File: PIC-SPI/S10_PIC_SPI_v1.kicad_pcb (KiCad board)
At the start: 2 copper layers, 254 x 134.1 mm, 164 parts, among them P1 M25P80 ISP, P10 CONN_4, P19 XILINX CABLE2, P2 CONN_4, P3 CONN_2, P4 S100_MALE, P5 PIC_ISP, P6 CONN_1, P7 CONN_1, P8 CONN_2, P9 CONN_2, Q1 ^^NPN-SOT23, Q2 ^^NPN-SOT23, Q3 ^^NPN-SOT23, Q4 ^^NPN-SOT23, Q5 ^^NPN-SOT23, Q6 ^^NPN-SOT23, Q7 ^^NPN-SOT23, Q8 ^^NPN-SOT23, Q9 ^^NPN-SOT23, SW1 RESET, SW2 RESET, SW4 FLASH_SELECT, SW50 FLASH/RUN, U1 LDO_REG_7805, U11 ^^74LS541, U12 ^^74LV244, U14 M25P80, U15 M25P80, U16 M25P80, U17 M25P80, U18 CH341A, U19 ^^74LS541, U2 LM1086CS, U20 XC95288XL-TQ144, U3din1 ^^74LS541, U3dout1 ^^74LS541, U4 ^^74LS541, U5 ^^74LS541, U6 ^^74LS541, U7a1 74HC245, U7b1 74HC245, U8 PIC18F1330, X1 12MHz

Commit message: PIC-SPI: annotate, add 7-segment displays (2x 74HC4511), read netlist into the PCB
Source: S100 PIC_SPI_v1/backups/06-01-2016 1810
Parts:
- removed Cx15: 0.1 uF, C2
- removed D13: POWER FT232R, ^^LED-0805
- removed D14: TMA0, ^^LED-0805
- removed D15: TMA1, ^^LED-0805
- removed D16: TMA2, ^^LED-0805
- removed D17: TMA3, ^^LED-0805
- removed D6: DONE, ^^LED-0805
- removed Dx2, Dx3: LED, ^^LED-0805
- removed JP4, JP5: JUMPER, PIN_ARRAY_2X1
- removed Jx1: USB_2, USB_A
- removed Kx1: CONN_3, SIL-3
- removed P3: CONN_2, SIL-2
- removed Px12: CLK_UART, DIP-14__300_ELL
- removed Q3, Q4, Q5, Q6, Q7, Q8, Q9: ^^NPN-SOT23, ^^-SOT23
- removed R45, Rx7, Rx8: 330, ^^SMD_Resistor-0805
- removed R46, R47: 470, ^^SMD_Resistor-0805
- removed Rx2: 4700, ^^SMD_Resistor-0805
- removed SW4: FLASH_SELECT, SW_PUSH_SMALL
- removed SWx2: DIPS_08, 16dip300
- removed U7a1, U7b1: 74HC245, ^^-SO20W
- removed Ux17: 74LS682N, 20DIP-ELL300
- removed Ux18: 16550, DIP-40__600_ELL
- removed Ux21: FT232R, -SSOP28
- added BAT1: CR2032, CR2032H, F.Cu at (165.0, 122.4)
- added C13: 0.01 uF, ^^SMD_Resistor-0805, B.Cu at (266.5, 101.6)
- added C16: 0.1 uF, C2, F.Cu at (158.6, 186.6)
- added C22: 0.1 uF, C2, F.Cu at (181.6, 150.3)
- added C23: 0.1 uF, C2, F.Cu at (125.2, 99.6)
- added C24: 0.1 uF, C2, F.Cu at (124.7, 186.5)
- added C29: 0.1 uF, C2, F.Cu at (124.8, 172.4)
- added C30: 0.1 uF, C2, F.Cu at (181.6, 165.3)
- added C31: 0.1 uF, ^^SMD_Resistor-0805, F.Cu at (200.3, 183.6)
- added C32: 0.1 uF, C2, F.Cu at (152.4, 143.9)
- added C41: 0.1 uF, ^^SMD_Resistor-0805, B.Cu at (227.6, 183.9)
- added C42: 0.1 uF, ^^SMD_Resistor-0805, B.Cu at (290.3, 199.5)
- added C43: 0.1 uF, ^^SMD_Resistor-0805, B.Cu at (290.4, 182.4)
- added IC1: MCP23S08SO, DIP-18__300_ELL, F.Cu at (195.9, 165.4)
- added IC2: MCP23S08SO, DIP-18__300_ELL, F.Cu at (195.9, 150.3)
- added JP1: JUMPER, SIL-2, F.Cu at (178.7, 201.4)
- added MCP1: CONN_3X2, PIN_ARRAY_3X2, F.Cu at (175.6, 156.7)
- added MCP2: CONN_3X2, PIN_ARRAY_3X2, F.Cu at (175.5, 164.4)
- added P11: CONN_3X2, PIN_ARRAY_3X2, F.Cu at (163.4, 174.8)
- added P12: CONN_8X2, pin_array_8x2, F.Cu at (139.9, 201.4)
- added P13: MCP_1, SIL-10, F.Cu at (190.7, 91.4)
- added P14: MCP_2, SIL-10, F.Cu at (190.7, 97.1)
- added RR1: 1000, r_pack9, F.Cu at (141.1, 107.6)
- added S1: 7SEGM, ^^VQB71_7segment, F.Cu at (310.0, 175.3)
- added S2: 7SEGM, ^^VQB71_7segment, F.Cu at (319.4, 175.2)
- added SW3: DIPS_08, SWDIP8, F.Cu at (110.1, 144.1)
- added SW5: DIPS_08, SWDIP8, F.Cu at (137.1, 144.2)
- added SW6: DIPS_08, SWDIP8, F.Cu at (109.7, 103.8)
- added U10: 74HC245, ^^-SO20W, F.Cu at (249.4, 183.8)
- added U13: 74LS244, DIP-20__300_ELL, F.Cu at (140.7, 99.6)
- added U21: 74LS240, DIP-20__300_ELL, F.Cu at (140.3, 186.7)
- added U22: DS1305, DIP-16__300_ELL, F.Cu at (165.4, 143.9)
- added U23: M25P80, -SO8, F.Cu at (296.2, 157.5)
- added U24: M25P80, -SO8, F.Cu at (304.6, 157.5)
- added U25: M25P80, -SO8, F.Cu at (312.8, 157.5)
- added U26: M25P80, -SO8, F.Cu at (320.8, 157.5)
- added U27: 74HC4511, ^^-SO16W, B.Cu at (290.2, 175.1)
- added U28: 74HC4511, ^^-SO16W, B.Cu at (290.1, 192.3)
- added U3: 74LS682N, DIP-20__300_ELL, F.Cu at (140.3, 158.2)
- added U30: 74HC04, DIP-14__300_ELL, F.Cu at (170.4, 186.6)
- added U31: ^^74LS541, ^^-SO20W, F.Cu at (208.5, 183.9)
- added U7: 74LS682N, DIP-20__300_ELL, F.Cu at (140.3, 172.5)
- added U9: 74HC245, ^^-SO20W, F.Cu at (228.2, 183.9)
- added X2: CRYSTAL, Crystal_HC-49U_Horiz, F.Cu at (163.7, 152.7)
- C10, C15, C18: moved to B.Cu
- C17, C20, C21, C25, C27, C28, C4, C8: footprint C2 -> ^^SMD_Resistor-0805
- D10: value FLASH_1 -> D1
- D11: value FLASH_2 -> D4
- D12: value FLASH_3 -> D5
- D2: value P55 -> D2
- D3: value P54 -> D3
- D9: value FLASH_0 -> D0
- R11: value 10k -> 1K; footprint ^^SMD_Resistor-0805 -> ^^R3; moved to F.Cu
- R31, R33, R35, R37, R39: value 330 -> 1K
- R32, R34, R36, R38: value 470 -> 1K
- R40, R41, R42, R43, R44: value 330 -> 1K; moved to B.Cu
- R6: value 330 -> 1K; footprint ^^SMD_Resistor-0805 -> ^^R3; moved to F.Cu
- R7: value 470 -> 50
- U11: value ^^74LS541 -> 8259A; footprint ^^-SO20W -> DIP-28__600_ELL
- U14: footprint 8DIP-ELL300 -> -SO8
- U15, U16, U17: moved to F.Cu
- U18: footprint -SO28W -> ^^-SO28W
- U3din1, U3dout1: value ^^74LS541 -> ^^74HC541
- moved R31 180.9 mm to (302.2, 177.3)
- moved R33 168.7 mm to (302.2, 172.8), turned to 180 degrees
- moved R32 167.7 mm to (302.2, 175.1), turned to 180 degrees
- moved R39 166.4 mm to (301.9, 191.9), turned to 180 degrees
- moved R38 164.3 mm to (301.9, 194.1), turned to 180 degrees
- moved R37 164.0 mm to (302.2, 179.5), turned to 180 degrees
- moved R35 162.6 mm to (302.2, 168.4), turned to 180 degrees
- moved R36 162.4 mm to (302.2, 181.7), turned to 180 degrees
- moved R34 161.6 mm to (302.2, 170.6), turned to 180 degrees
- moved P19 147.2 mm to (233.8, 93.0), turned to 180 degrees
- moved R40 145.2 mm to (302.0, 189.6), turned to 180 degrees
- moved R27 143.5 mm to (236.4, 98.4), turned to 90 degrees
- moved R41 142.8 mm to (302.0, 187.4), turned to 180 degrees
- moved R25 141.2 mm to (233.8, 98.4), turned to 90 degrees
- moved R42 140.5 mm to (302.0, 185.2), turned to 180 degrees
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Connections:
- net /DI0b renamed /DI0
- net /DI1b renamed /DI1
- net /DI2b renamed /DI2
- net /DI3b renamed /DI3
- net /DI4b renamed /DI4
- net /DI5b renamed /DI5
- net /DI6b renamed /DI6
- net /DI7b renamed /DI7
- net /DO0b renamed /DO0
- net /DO1b renamed /DO1
- net /DO2b renamed /DO2
- net /DO3b renamed /DO3
- net /DO4b renamed /DO4
- net /DO5b renamed /DO5
- net /DO6b renamed /DO6
- net /DO7b renamed /DO7
- net /FLASH_0 renamed /LED_D0
- net /FLASH_1 renamed /LED_D1
- C14 pad 1: /V3.3b -> GND
- C14 pad 2: GND -> N-00000116
- C19 pad 1: /V3.3 -> /V3.3_CLPD_IO
- C26 pad 1: /V3.3 -> /V3.3_CLPD_INT
- C33 pad 1: /V3.3 -> /V3.3_CLPD_INT
- C34 pad 1: /V3.3 -> /V3.3_CLPD_IO
- C35 pad 1: /V3.3 -> /V3.3_CLPD_IO
- C36 pad 1: /V3.3 -> /V3.3_CLPD_IO
- C37 pad 1: /V3.3 -> /V3.3_CLPD_IO
- C38 pad 1: /V3.3 -> /V3.3_CLPD_IO
- C39 pad 1: /V3.3 -> /V3.3_CLPD_IO
- C40 pad 1: /V3.3 -> /V3.3_CLPD_IO
- D11 pad 1: /FLASH_2 -> /LED_D4
- D12 pad 1: /FLASH_3 -> /LED_D5
- D2 pad 1: N-00000404 -> /LED_D2
- D2 pad 2: GND -> N-00000211
- D3 pad 1: N-00000407 -> /LED_D3
- D3 pad 2: GND -> N-00000212
- D7 pad 1: N-00000403 -> /BOARD_SEL_LED
- D7 pad 2: GND -> N-00000256
- JPx1 pad 2: /BOARD_INTERRUPT_VECTc -> /BOARD_INTERRUPT_VECTb
- JPx2 pad 2: /BOARD_INTERRUPT_VECTc -> /BOARD_INTERRUPT_VECTb
- JPx3 pad 2: /BOARD_INTERRUPT_VECTc -> /BOARD_INTERRUPT_VECTb
- JPx4 pad 2: /BOARD_INTERRUPT_VECTc -> /BOARD_INTERRUPT_VECTb
- JPx5 pad 2: /BOARD_INTERRUPT_VECTc -> /BOARD_INTERRUPT_VECTb
- JPx6 pad 2: /BOARD_INTERRUPT_VECTc -> /BOARD_INTERRUPT_VECTb
- JPx7 pad 2: /BOARD_INTERRUPT_VECTc -> /BOARD_INTERRUPT_VECTb
- JPx8 pad 2: /BOARD_INTERRUPT_VECTc -> /BOARD_INTERRUPT_VECTb
- P4 pad 15: /A18b -> /A18
- P4 pad 16: /A16b -> /A16
- P4 pad 17: /A17b -> /A17
- P4 pad 29: /A5b -> /A5
- P4 pad 30: /A4b -> /A4
- P4 pad 31: /A3b -> /A3
- P4 pad 32: /A15b -> /A15
- P4 pad 33: /A12b -> /A12
- P4 pad 34: /A9b -> /A9
- P4 pad 37: /A10b -> /A10
- P4 pad 58: (no net) -> /sXTRQ*
- P4 pad 59: /A19b -> /A19
- P4 pad 61: /A20b -> /A20
- P4 pad 62: /A21b -> /A21
- P4 pad 63: /A22b -> /A22
- P4 pad 64: /A23b -> /A23
- P4 pad 72: /RDY -> (no net)
- P4 pad 73: (no net) -> /INT*
- P4 pad 79: /A0b -> /A0
- P4 pad 80: /A1b -> /A1
- P4 pad 81: /A2b -> /A2
- P4 pad 82: /A6b -> /A6
- P4 pad 83: /A7b -> /A7
- P4 pad 84: /A8b -> /A8
- P4 pad 85: /A13b -> /A13
- P4 pad 86: /A14b -> /A14
- P4 pad 87: /A11b -> /A11
- P4 pad 96: (no net) -> /sINTA
- P8 pad 1: /V3.3 -> /V3.3_CLPD_INT
- P9 pad 1: /V3.3 -> /V3.3_CLPD_IO
- R11 pad 2: N-00000274 -> N-00000236
- R13 pad 1: N-00000404 -> GND
- R13 pad 2: /LED_D2 -> N-00000211
- R15 pad 1: N-00000228 -> GND
- R16 pad 1: N-00000407 -> GND
- R16 pad 2: /LED_D3 -> N-00000212
- R20 pad 1: N-00000403 -> GND
- R20 pad 2: /BOARD_SEL_LED -> N-00000256
- R31 pad 2: GND -> N-00000221
- R32 pad 1: /TMA0* -> N-00000271
- R33 pad 2: VCC -> N-00000244
- R34 pad 1: /TMA1* -> N-00000263
- R35 pad 2: VCC -> N-00000245
- R36 pad 1: /TMA2* -> N-00000265
- R37 pad 2: VCC -> N-00000247
- R38 pad 1: /TMA3* -> N-00000258
- R39 pad 2: VCC -> N-00000250
- R40 pad 1: /TMA0* -> N-00000269
- R40 pad 2: VCC -> N-00000251
- R41 pad 1: /TMA1* -> N-00000268
- R41 pad 2: VCC -> N-00000252
- R42 pad 1: /TMA2* -> N-00000267
- R42 pad 2: VCC -> N-00000253
- R43 pad 1: /TMA3* -> N-00000259
- R43 pad 2: VCC -> N-00000254
- R44 pad 2: VCC -> N-00000255
- R6 pad 1: N-00000388 -> N-00000210
- R7 pad 1: N-00000390 -> /MCP_AddrHi
- R7 pad 2: /DONE_LED -> /V3.3
- U11 pad 1: GND -> /out8259CS*bufferedViaU31
- U11 pad 10: GND -> /D1
- U11 pad 11: (no net) -> /D0
- U11 pad 14: (no net) -> GND
- U11 pad 15: /TMA3* -> (no net)
- U11 pad 16: /TMA2* -> N-00000210
- U11 pad 17: /TMA1* -> N-00000272
- U11 pad 18: /TMA0* -> /VI0
- U11 pad 19: GND -> /VI1
- U11 pad 2: /TMA0_CPLD -> /pWR*b
- U11 pad 20: VCC -> /VI2
- U11 pad 3: /TMA1_CPLD -> /pDBIN*b
- U11 pad 4: /TMA2_CPLD -> /D7
- U11 pad 5: /TMA3_CPLD -> /D6
- U11 pad 6: (no net) -> /D5
- U11 pad 7: (no net) -> /D4
- U11 pad 8: (no net) -> /D3
- U11 pad 9: (no net) -> /D2
- U12 pad 14: /FLASH_CS -> /25Pxx_CS
- U12 pad 5: /FLASH_CS -> /25Pxx_CS
- U14 pad 1: /FLASH_SEL_0 -> /25Pxx_SEL_0
- U15 pad 1: /FLASH_SEL_1 -> /25Pxx_SEL_1
- U16 pad 1: /FLASH_SEL_2 -> /25Pxx_SEL_2
- U17 pad 1: /FLASH_SEL_3 -> /25Pxx_SEL_3
- U18 pad 2: (no net) -> N-00000138
- U18 pad 9: /V3.3b -> N-00000116
- U2 pad 4: (no net) -> /V3.3
- U20 pad 1: /V3.3 -> /V3.3_CLPD_IO
- U20 pad 109: /V3.3 -> /V3.3_CLPD_IO
- U20 pad 124: (no net) -> /25Pxx_CS
- U20 pad 125: (no net) -> /25Pxx_SEL_0
- U20 pad 126: (no net) -> /25Pxx_SEL_1
- U20 pad 127: /V3.3 -> /V3.3_CLPD_IO
- U20 pad 128: (no net) -> /25Pxx_SEL_2
- U20 pad 129: (no net) -> /25Pxx_SEL_3
- U20 pad 139: (no net) -> /SPI_CLK
- U20 pad 140: (no net) -> /SPI_Din
- U20 pad 141: /V3.3 -> /V3.3_CLPD_INT
- U20 pad 142: (no net) -> /SPI_Dout
- U20 pad 143: (no net) -> /BOARD_INTERRUPT_VECTb
- U20 pad 17: /D0 -> (no net)
- U20 pad 19: /D1 -> (no net)
- U20 pad 2: //WAITtoS100 -> (no net)
- U20 pad 20: //M1 -> /sINTAb
- U20 pad 23: (no net) -> /sXTRQ*b
- U20 pad 25: //CS_UART -> /SPI_CS_00
- U20 pad 26: (no net) -> /SPI_CS_01
- U20 pad 27: (no net) -> /SPI_CS_02
- U20 pad 3: /RESETtoS100 -> /RESET*b
- U20 pad 30: /DONE_LED -> (no net)
- U20 pad 37: /V3.3 -> /V3.3_CLPD_IO
- U20 pad 4: /~UART_INT -> /7SEG_0_D0
- U20 pad 42: /V3.3 -> /V3.3_CLPD_INT
- U20 pad 43: (no net) -> //M1
- U20 pad 44: (no net) -> /Z80intVectorBusout
- U20 pad 5: /BOARD_INTERRUPT_VECT -> /7SEG_0_D1
- U20 pad 55: /V3.3 -> /V3.3_CLPD_IO
- U20 pad 56: N-0000011 -> /25Pxx_SEL_4
- U20 pad 57: /FLASH_CS -> /25Pxx_SEL_5
- U20 pad 58: /Q2 -> /25Pxx_SEL_6
- U20 pad 59: /Q1 -> /25Pxx_SEL_7
- U20 pad 6: /LED_D3 -> /7SEG_0_D2
- U20 pad 60: /FLASH_SEL_3 -> /7SEG_1_D3
- U20 pad 61: /FLASH_SEL_2 -> /7SEG_1_D2
- U20 pad 64: /FLASH_SEL_1 -> /7SEG_1_D1
- U20 pad 66: /FLASH_SEL_0 -> /7SEG_1_D0
- U20 pad 68: /PIC18F_0 -> (no net)
- U20 pad 69: /PIC18F_1 -> /in8259CS*
- U20 pad 7: /LED_D2 -> /7SEG_0_D3
- U20 pad 70: /PIC18F_2 -> /out8259CS*
- U20 pad 73: /V3.3 -> /V3.3_CLPD_IO
- U20 pad 75: /FLASH_2 -> /LED_D2
- U20 pad 76: /FLASH_3 -> /LED_D3
- U20 pad 77: (no net) -> /LED_D4
- U20 pad 78: (no net) -> /LED_D5
- U20 pad 8: /V3.3 -> /V3.3_CLPD_INT
- U20 pad 84: /V3.3 -> /V3.3_CLPD_INT
- U4 pad 11: /A7 -> /A7b
- U4 pad 12: /A6 -> /A6b
- U4 pad 13: /A5 -> /A5b
- U4 pad 14: /A4 -> /A4b
- U4 pad 15: /A3 -> /A3b
- U4 pad 16: /A2 -> /A2b
- U4 pad 17: /A1 -> /A1b
- U4 pad 18: /A0 -> /A0b
- U4 pad 2: /A0b -> /A0
- U4 pad 3: /A1b -> /A1
- U4 pad 4: /A2b -> /A2
- U4 pad 5: /A3b -> /A3
- U4 pad 6: /A4b -> /A4
- U4 pad 7: /A5b -> /A5
- U4 pad 8: /A6b -> /A6
- U4 pad 9: /A7b -> /A7
- U5 pad 11: /A15 -> /A15b
- U5 pad 12: /A14 -> /A14b
- U5 pad 13: /A13 -> /A13b
- U5 pad 14: /A12 -> /A12b
- U5 pad 15: /A11 -> /A11b
- U5 pad 16: /A10 -> /A10b
- U5 pad 17: /A9 -> /A9b
- U5 pad 18: /A8 -> /A8b
- U5 pad 2: /A8b -> /A8
- U5 pad 3: /A9b -> /A9
- U5 pad 4: /A10b -> /A10
- U5 pad 5: /A11b -> /A11
- U5 pad 6: /A12b -> /A12
- U5 pad 7: /A13b -> /A13
- U5 pad 8: /A14b -> /A14
- U5 pad 9: /A15b -> /A15
- U6 pad 11: /A23 -> (no net)
- U6 pad 12: /A22 -> (no net)
- U6 pad 13: /A21 -> (no net)
- U6 pad 14: /A20 -> (no net)
- U6 pad 15: /A19 -> (no net)
- U6 pad 16: /A18 -> (no net)
- U6 pad 17: /A17 -> (no net)
- U6 pad 18: /A16 -> (no net)
- U6 pad 2: /A16b -> /A16
- U6 pad 3: /A17b -> /A17
- U6 pad 4: /A18b -> /A18
- U6 pad 5: /A19b -> /A19
- U6 pad 6: /A20b -> /A20
- U6 pad 7: /A21b -> /A21
- U6 pad 8: /A22b -> /A22
- U6 pad 9: /A23b -> /A23
- U8 pad 10: /PIC18F_1 -> (no net)
- U8 pad 11: /PIC18F_0 -> (no net)
- U8 pad 18: N-00000274 -> (no net)
- U8 pad 7: /PIC18F_2 -> (no net)
- Ux1 pad 4: /V3.3b -> (no net)
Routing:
- net /+8V: track 0.00 -> 70.1 mm
- net /V3.3: track 0.00 -> 34.9 mm
- net VCC: track 0.00 -> 27.1 mm
- net /Q2: track 0.00 -> 19.6 mm, vias 0 -> 2
- net /Q1: track 0.00 -> 13.5 mm, vias 0 -> 2
- net N-00000114: track 0.00 -> 12.9 mm
- net N-00000115: track 0.00 -> 10.2 mm
- net N-00000317: track 0.00 -> 9.22 mm, vias 0 -> 1
- net N-00000309: track 0.00 -> 6.99 mm, vias 0 -> 1
- net N-00000138: track 0.00 -> 6.89 mm
- net N-00000384: track 0.00 -> 6.29 mm
- net N-00000381: track 0.00 -> 6.15 mm
- net N-0000084: track 0.00 -> 5.81 mm
- net N-00000200: track 0.00 -> 5.47 mm, vias 0 -> 1
- net N-00000351: track 0.00 -> 5.40 mm, vias 0 -> 1
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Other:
- net class Default: trace_width 0.25 -> 0.23
- net class Power 3v added: clearance 0.22, trace_width 0.35, via_dia 1.143, via_drill 0.635
- board text added: "BOARD"
- board text added: "Incomming Interrupt Channels"
- board text added: "Q1"
- board text added: "Q2"
- board text removed: "CLK UART"
- board text removed: "F_SEL"
- board text removed: "RDY (P72)"
- board text removed: "RESET (P75)"
- board text removed: "RX"
- board text removed: "TX"
- board text removed: "U11"
- board text removed: "U7a1"
- board text removed: "U7b1"
- board text removed: "~UART INT"
- board text removed: "~VIx"

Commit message: PIC-SPI: add CPLD I/O header P2 and EXT SPI header P3, drop debug LEDs; placement
Source: S100 PIC_SPI_v1/backups/07-01-2016 1914
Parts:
- removed D10: D1, ^^LED-0805
- removed D11: D4, ^^LED-0805
- removed D12: D5, ^^LED-0805
- removed D2: D2, ^^LED-0805
- removed D3: D3, ^^LED-0805
- removed P10: CONN_4, SIL-4
- removed R13, R16, R22, R23, R24: 330, ^^SMD_Resistor-0805
- added P3: EXT SPI, PIN_ARRAY_4X2, F.Cu at (196.6, 91.2)
- BAT1: footprint CR2032H -> ^^CR2032H
- C8, U19: moved to F.Cu
- P2: value CONN_4 -> CONN_8X2; footprint SIL-4 -> PIN_ARRAY_8x2
- R10, R14, R9: moved to B.Cu
- moved C6 155.0 mm to (97.0, 123.6)
- moved R7 96.8 mm to (117.4, 95.6)
- moved C30 91.1 mm to (117.4, 100.8)
- moved IC1 91.1 mm to (131.6, 100.8)
- moved MCP2 90.2 mm to (110.6, 101.8)
- moved MCP1 90.2 mm to (110.5, 94.3)
- moved SW6 83.4 mm to (172.7, 158.4)
- moved C23 80.3 mm to (158.6, 172.6)
- moved U13 80.3 mm to (174.1, 172.6)
- moved R21 79.9 mm to (211.3, 90.4), turned to 90 degrees
- moved D9 76.9 mm to (211.3, 90.4), turned to 90 degrees
- moved D7 68.6 mm to (206.8, 90.5)
- moved R20 63.2 mm to (206.8, 90.5)
- moved C22 59.0 mm to (149.6, 100.7)
- moved IC2 59.0 mm to (163.8, 100.7)
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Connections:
- net N-00000261 renamed /Vbat
- C22 pad 1: VCC -> /V3.3
- C30 pad 1: VCC -> /V3.3
- C32 pad 1: VCC -> /V3.3
- C32 pad 2: GND -> (no net)
- D9 pad 1: /LED_D0 -> /CPLD_68
- P2 pad 1: GND -> /V3.3
- P2 pad 2: N-0000056 -> VCC
- P2 pad 3: N-0000051 -> GND
- P2 pad 4: N-0000055 -> GND
- U19 pad 11: /D7 -> /D0
- U19 pad 12: /D6 -> /D1
- U19 pad 13: /D5 -> /D2
- U19 pad 14: /D4 -> /D3
- U19 pad 15: /D3 -> /D4
- U19 pad 16: /D2 -> /D5
- U19 pad 17: /D1 -> /D6
- U19 pad 18: /D0 -> /D7
- U19 pad 2: /CPLD_45 -> /CPLD_133
- U19 pad 3: /CPLD_46 -> /CPLD_132
- U19 pad 4: /CPLD_48 -> /CPLD_131
- U19 pad 5: /CPLD_49 -> /CPLD_130
- U19 pad 6: /CPLD_130 -> /CPLD_49
- U19 pad 7: /CPLD_131 -> /CPLD_48
- U19 pad 8: /CPLD_132 -> /CPLD_46
- U19 pad 9: /CPLD_133 -> /CPLD_45
- U20 pad 100: /A0 -> /CPLD_71
- U20 pad 101: /A1 -> /CPLD_74
- U20 pad 102: /A2 -> /CPLD_75
- U20 pad 103: /A3 -> /CPLD_76
- U20 pad 104: /A4 -> /CPLD_77
- U20 pad 105: /A5 -> /CPLD_78
- U20 pad 106: /A6 -> /7SEG_1_D0
- U20 pad 107: /A7 -> /7SEG_1_D1
- U20 pad 110: N-0000052 -> /BOARD_INTERRUPT_VECTb
- U20 pad 111: N-0000053 -> /TMA0_CPLD
- U20 pad 112: N-0000054 -> /TMA1_CPLD
- U20 pad 113: N-0000055 -> /TMA2_CPLD
- U20 pad 115: N-0000051 -> /TMA3_CPLD
- U20 pad 116: N-0000056 -> /A23
- U20 pad 117: /TMA0_CPLD -> /A0
- U20 pad 118: /TMA1_CPLD -> /A1
- U20 pad 119: /TMA2_CPLD -> /A2
- U20 pad 120: /TMA3_CPLD -> /A3
- U20 pad 121: (no net) -> /A4
- U20 pad 124: /25Pxx_CS -> /A5
- U20 pad 125: /25Pxx_SEL_0 -> /A6
- U20 pad 126: /25Pxx_SEL_1 -> /A7
- U20 pad 128: /25Pxx_SEL_2 -> /A8
- U20 pad 129: /25Pxx_SEL_3 -> /A9
- U20 pad 130: /CPLD_130 -> /A10
- U20 pad 131: /CPLD_131 -> /A11
- U20 pad 132: /CPLD_132 -> /A12
- U20 pad 133: /CPLD_133 -> /A13
- U20 pad 134: /CPLD_134 -> /A14
- U20 pad 135: /CPLD_M25P80_CLK -> /A15
- U20 pad 136: /CPLD_M25P80_Din -> /A16
- U20 pad 137: /CPLD_M25P80_CS -> /A17
- U20 pad 138: /CPLD_M25P80_Dout -> /A18
- U20 pad 139: /SPI_CLK -> /A19
- U20 pad 140: /SPI_Din -> /A20
- U20 pad 142: /SPI_Dout -> /A21
- U20 pad 143: /BOARD_INTERRUPT_VECTb -> /A22
- U20 pad 17: (no net) -> /SPI_CS_03
- U20 pad 4: /7SEG_0_D0 -> /PHIb
- U20 pad 5: /7SEG_0_D1 -> /CLOCK*b
- U20 pad 50: /pWR*b -> /CPLD_130
- U20 pad 51: /pDBINb -> /CPLD_131
- U20 pad 52: /sWO*b -> /CPLD_132
- U20 pad 53: /CLOCK*b -> /CPLD_133
- U20 pad 54: /PHIb -> /CPLD_134
- U20 pad 56: /25Pxx_SEL_4 -> /pWR*b
- U20 pad 57: /25Pxx_SEL_5 -> /SPI_CLK
- U20 pad 58: /25Pxx_SEL_6 -> /SPI_Din
- U20 pad 59: /25Pxx_SEL_7 -> /SPI_Dout
- U20 pad 6: /7SEG_0_D2 -> /sWO*b
- U20 pad 60: /7SEG_1_D3 -> /CPLD_M25P80_CLK
- U20 pad 61: /7SEG_1_D2 -> /CPLD_M25P80_Din
- U20 pad 64: /7SEG_1_D1 -> /CPLD_M25P80_CS
- U20 pad 66: /7SEG_1_D0 -> /CPLD_M25P80_Dout
- U20 pad 68: (no net) -> /CPLD_68
- U20 pad 7: /7SEG_0_D3 -> /pDBINb
- U20 pad 71: /LED_D0 -> (no net)
- U20 pad 74: /LED_D1 -> /7SEG_0_D0
- U20 pad 75: /LED_D2 -> /7SEG_0_D1
- U20 pad 76: /LED_D3 -> /7SEG_0_D2
- U20 pad 77: /LED_D4 -> /7SEG_0_D3
- U20 pad 78: /LED_D5 -> (no net)
- U20 pad 79: /A8 -> /25Pxx_CS
- U20 pad 80: /A9 -> /25Pxx_SEL_0
- U20 pad 81: /A10 -> /25Pxx_SEL_1
- U20 pad 82: /A11 -> /25Pxx_SEL_2
- U20 pad 83: /A12 -> /25Pxx_SEL_3
- U20 pad 85: /A13 -> /25Pxx_SEL_4
- U20 pad 86: /A14 -> /25Pxx_SEL_5
- U20 pad 87: /A15 -> /25Pxx_SEL_6
- U20 pad 88: /A16 -> /25Pxx_SEL_7
- U20 pad 91: /A17 -> /7SEG_1_D2
- U20 pad 92: /A18 -> /7SEG_1_D3
- U20 pad 93: /A19 -> /CPLD_116
- U20 pad 94: /A20 -> /CPLD_115
- U20 pad 95: /A21 -> /CPLD_113
- U20 pad 96: /A22 -> /CPLD_112
- U20 pad 97: /A23 -> /CPLD_111
- U20 pad 98: (no net) -> /CPLD_110
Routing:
- net /V3.3: track 34.9 -> 41.1 mm
- net N-00000142: track 10.2 -> 12.7 mm
- net N-00000141: track 12.9 -> 13.6 mm
- removed copper zone on B.Cu, net GND
- removed copper zone on F.Cu, net GND
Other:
- net class Power 3v: trace_width 0.35 -> 0.45; via_dia 1.143 -> 0.889; via_drill 0.635 -> 0.5842
- net class power 5v: via_dia 1.143 -> 0.889; via_drill 0.635 -> 0.5842
- board text added: "3.3V GND P78 P77 P76 P75 P74 P71"
- board text added: "5V GND P116 P115 P113 P112 P111 P110"
- board text added: "BS"
- board text added: "D0"
- board text added: "RUN/PROG"
- board text removed: "B_S"
- board text removed: "D2"
- board text removed: "D3"
- board text removed: "F0 F1 F2 F3"
- board text removed: "GND P110 P111 P112"
- board text removed: "GND P116 P115 P113"
- board text removed: "RUN/FLASH"

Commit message: PIC-SPI: rip up tracks for a reroute
Source: S100 PIC_SPI_v1/backups/09-01-2016 1434 reroute
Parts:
- moved C43 42.7 mm to (286.8, 198.0), turned to 180 degrees
- moved U27 37.8 mm to (286.6, 191.0), turned to 90 degrees
- moved U28 37.2 mm to (286.8, 177.2), turned to 90 degrees
- moved C42 36.6 mm to (286.8, 183.9), turned to 180 degrees
- moved R36 30.8 mm to (299.9, 197.6), turned to 180 degrees
- moved R37 28.3 mm to (299.9, 195.4), turned to 180 degrees
- moved R31 25.9 mm to (299.9, 193.2), turned to 180 degrees
- moved R32 23.5 mm to (299.9, 190.9), turned to 180 degrees
- moved R42 22.6 mm to (299.9, 168.8), turned to 180 degrees
- moved R33 21.5 mm to (299.9, 188.7), turned to 180 degrees
- moved R41 20.7 mm to (299.9, 171.0), turned to 180 degrees
- moved R34 19.7 mm to (299.9, 186.4), turned to 180 degrees
- moved R40 19.1 mm to (299.9, 173.3), turned to 180 degrees
- moved R35 18.3 mm to (299.9, 184.3), turned to 180 degrees
- moved R39 18.0 mm to (299.9, 175.5), turned to 180 degrees
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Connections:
- U20 pad 116: /A23 -> /A23b
- U20 pad 117: /A0 -> /A0b
- U20 pad 118: /A1 -> /A1b
- U20 pad 119: /A2 -> /A2b
- U20 pad 120: /A3 -> /A3b
- U20 pad 121: /A4 -> /A4b
- U20 pad 124: /A5 -> /A5b
- U20 pad 125: /A6 -> /A6b
- U20 pad 126: /A7 -> /A7b
- U20 pad 128: /A8 -> /A8b
- U20 pad 129: /A9 -> /A9b
- U20 pad 130: /A10 -> /A10b
- U20 pad 131: /A11 -> /A11b
- U20 pad 132: /A12 -> /A12b
- U20 pad 133: /A13 -> /A13b
- U20 pad 134: /A14 -> /A14b
- U20 pad 135: /A15 -> /A15b
- U20 pad 136: /A16 -> /A16b
- U20 pad 137: /A17 -> /A17b
- U20 pad 138: /A18 -> /A18b
- U20 pad 139: /A19 -> /A19b
- U20 pad 140: /A20 -> /A20b
- U20 pad 142: /A21 -> /A21b
- U20 pad 143: /A22 -> /A22b
- U6 pad 11: (no net) -> /A23b
- U6 pad 12: (no net) -> /A22b
- U6 pad 13: (no net) -> /A21b
- U6 pad 14: (no net) -> /A20b
- U6 pad 15: (no net) -> /A19b
- U6 pad 16: (no net) -> /A18b
- U6 pad 17: (no net) -> /A17b
- U6 pad 18: (no net) -> /A16b
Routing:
- net /Q2: track 19.6 -> 0.00 mm, vias 2 -> 0
- net N-00000110: track 13.6 -> 0.00 mm
- net /Q1: track 13.5 -> 0.00 mm, vias 2 -> 0
- net N-00000111: track 12.7 -> 0.00 mm
- net N-00000284: track 9.22 -> 0.00 mm, vias 1 -> 0
- net N-00000280: track 6.99 -> 0.00 mm, vias 1 -> 0
- net N-00000242: track 6.89 -> 0.00 mm
- net N-00000377: track 6.29 -> 0.00 mm
- net /V3.3: track 41.1 -> 34.9 mm
- net N-00000378: track 6.15 -> 0.00 mm
- net N-0000076: track 5.81 -> 0.00 mm
- net N-00000103: track 5.47 -> 0.00 mm, vias 1 -> 0
- net N-0000075: track 5.07 -> 0.00 mm
- net VCC: track 27.1 -> 31.7 mm
- net N-00000106: track 4.52 -> 0.00 mm, vias 1 -> 0
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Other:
- net class Default: trace_width 0.23 -> 0.24

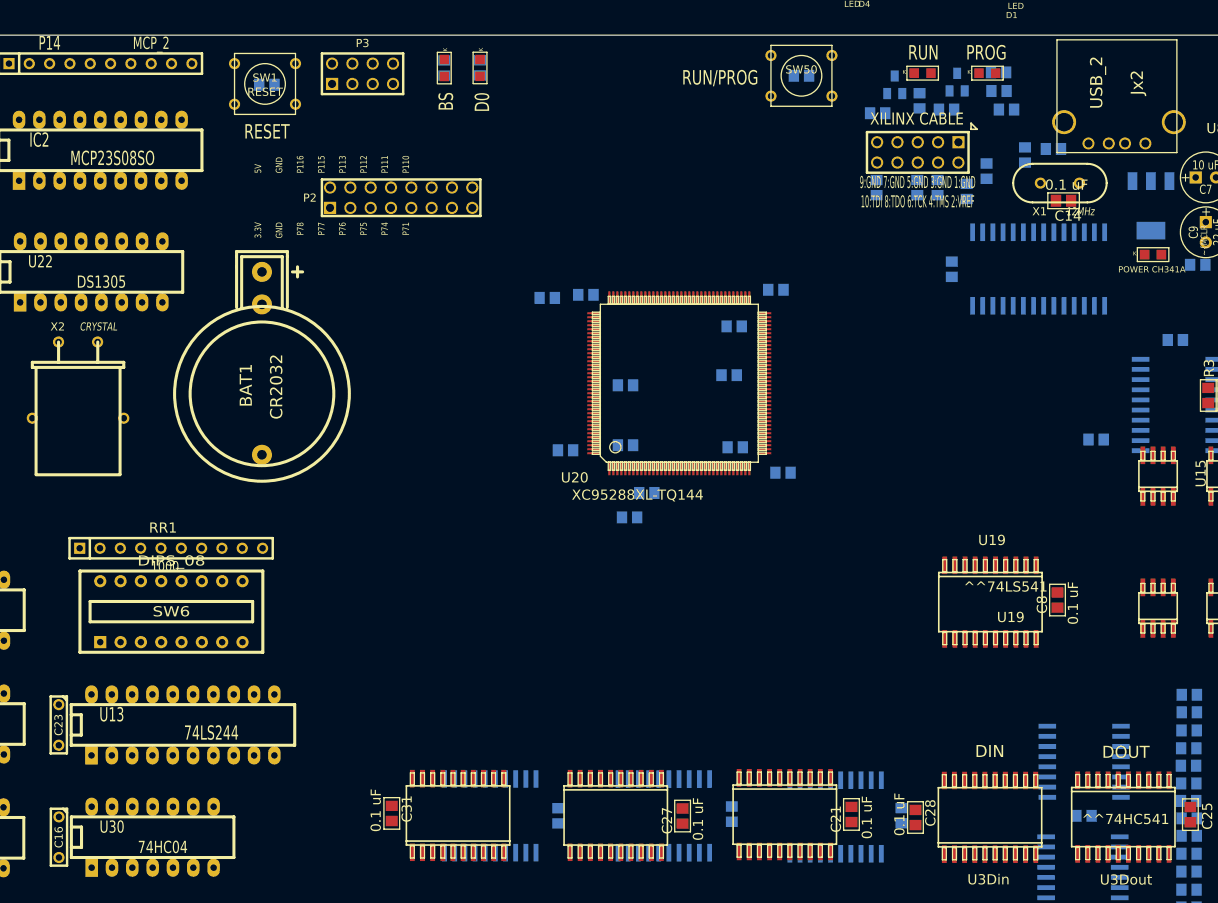
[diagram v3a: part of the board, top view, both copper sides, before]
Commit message: PIC-SPI: schematic wiring fix, pre-route tracks before autorouting
Source: S100 PIC_SPI_v1/backups/09-01-2016 1545
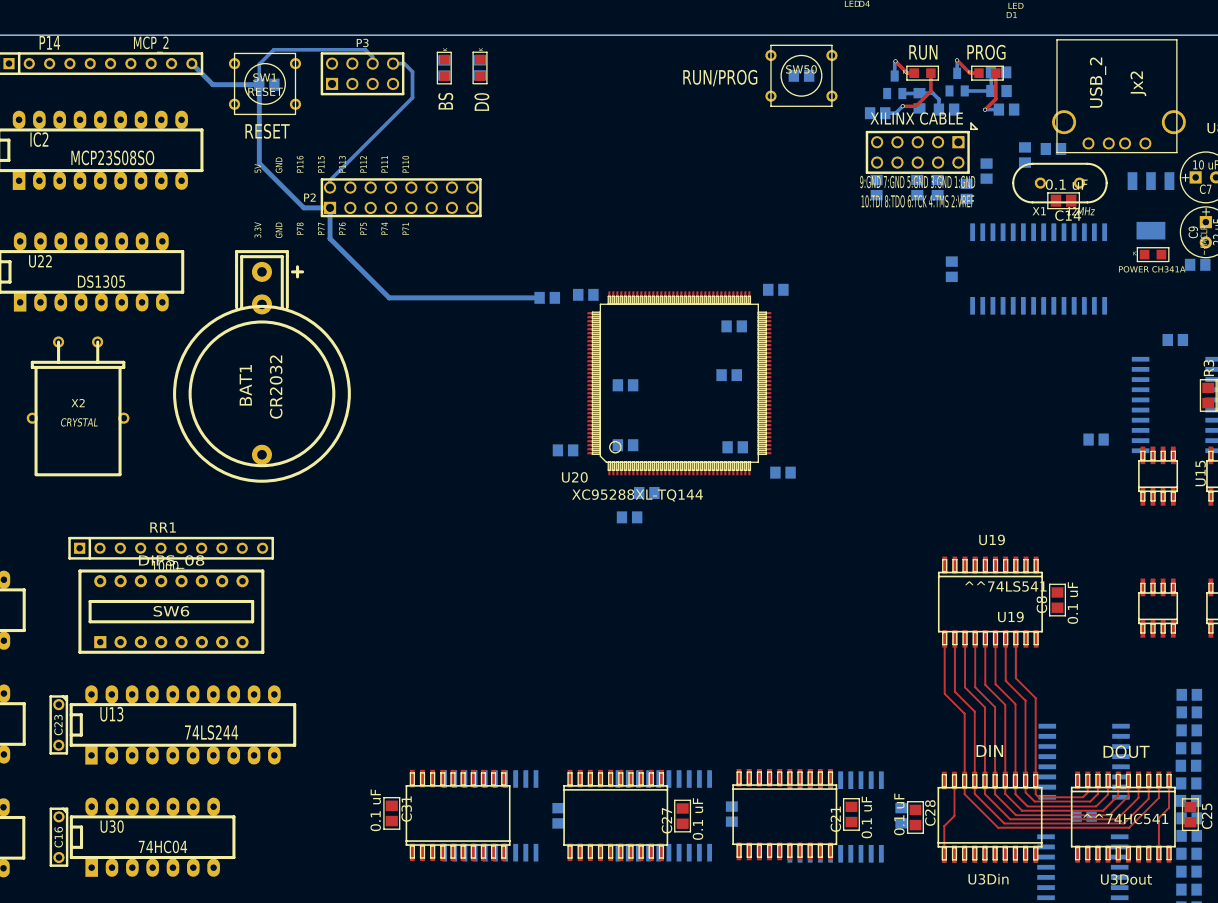
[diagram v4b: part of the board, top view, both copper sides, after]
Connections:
- C32 pad 2: (no net) -> GND
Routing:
- net /V3.3: track 34.9 -> 117.2 mm
- net /D0: track 0.00 -> 50.2 mm
- net /D1: track 0.00 -> 47.3 mm
- net /D2: track 0.00 -> 44.2 mm
- net /D3: track 0.00 -> 41.2 mm
- net /D4: track 0.00 -> 38.1 mm
- net /D5: track 0.00 -> 35.0 mm
- net /D6: track 0.00 -> 31.8 mm
- net /D7: track 0.00 -> 28.9 mm
- net VCC: track 31.7 -> 53.3 mm
- net /DBUSIN_EN: track 0.00 -> 9.73 mm
- net /DBUSOUT_EN: track 0.00 -> 9.73 mm
- net N-00000283: track 0.00 -> 9.11 mm, vias 0 -> 1
- net N-00000279: track 0.00 -> 6.87 mm, vias 0 -> 1
- net N-00000377: track 0.00 -> 6.19 mm
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
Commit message: PIC-SPI: autorouted layout (5100 tracks, 449 vias), manual track tweaks
Source: S100 PIC_SPI_v1 (working folder)
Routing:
- net GND: track 0.00 -> 1582.5 mm, vias 0 -> 37
- net VCC: track 53.3 -> 766.1 mm, vias 0 -> 6
- net /V3.3: track 117.2 -> 566.2 mm, vias 0 -> 2
- net /pWR*b: track 0.00 -> 249.2 mm, vias 0 -> 3
- net /D5: track 35.0 -> 256.3 mm, vias 0 -> 6
- net /D7: track 28.9 -> 244.6 mm, vias 0 -> 4
- net /D4: track 38.1 -> 252.7 mm, vias 0 -> 4
- net /D6: track 31.8 -> 242.6 mm, vias 0 -> 4
- net /D3: track 41.2 -> 251.4 mm, vias 0 -> 2
- net /DI2: track 0.00 -> 201.8 mm, vias 0 -> 6
- net /DI3: track 0.00 -> 199.4 mm, vias 0 -> 6
- net /A0b: track 0.00 -> 191.2 mm, vias 0 -> 2
- net /D2: track 44.2 -> 230.6 mm, vias 0 -> 2
- net /D1: track 47.3 -> 229.3 mm, vias 0 -> 2
- net /DI1: track 0.00 -> 180.8 mm, vias 0 -> 4
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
